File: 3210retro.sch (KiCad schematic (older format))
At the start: 11 parts, among them P101 USB_OTG, P102 NIMH, P103 LIPO, P104 DC, P105 EAR, P106 SPEAKER, P107 HEADPHONE, P108 RUMBLE, X101 ANT_GPS, X102 ANT_GSM

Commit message: Modification for STM32 adaption
For the Hackaday Prize 2017 I decided to switch to STM32 as CPU

*Power system was modified to just contain the charge IC,
*Boost converter for high voltage peripherals
*Buck converter for 3V3 for CPU and switchable NVCC_3V3
   for peripherie

CPU signals are routed and pinmux is done in firmware folder.

SD-Card has 4bit Interface

WiFi module ESP8266 is connected via UART

Wolfson Ausio codec is connected via SAI

Two digital microphones for noise canceling

Rumble Motor driver

LCD is connected via it's own I2C interface
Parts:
- removed P102: NIMH, Pin_Headers:Pin_Header_Straight_2x01, symbol CONN_01X02
- added TP101: TP, NokiaRetroFit:TP, symbol TP
- R101: footprint Resistors_SMD:R_0402 -> Resistors_SMD:R_0402_NoSilk
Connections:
- wire segments 61 -> 85
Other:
- note added: "CPU"
- note added: "Debug UART Output"
- note added: "IMU"
- note added: "Power management and battery charger circuit"
- note added: "SD-Card"
- note removed: "11"
- note removed: "12"
- note removed: "13"
- note removed: "8,9,10,11,12,13"
- note removed: "Battery selection and power domain overview"
- note removed: "CPU mainsheet"
- note removed: "DDR3 RAM"
- note removed: "SD interface / eMMC"
- note removed: "USB / IMU (gyro, accel, comp)"
- note removed: "i.MX7 PMIC"
- note removed: "i.MX7 power"
- moved on the sheet: P103

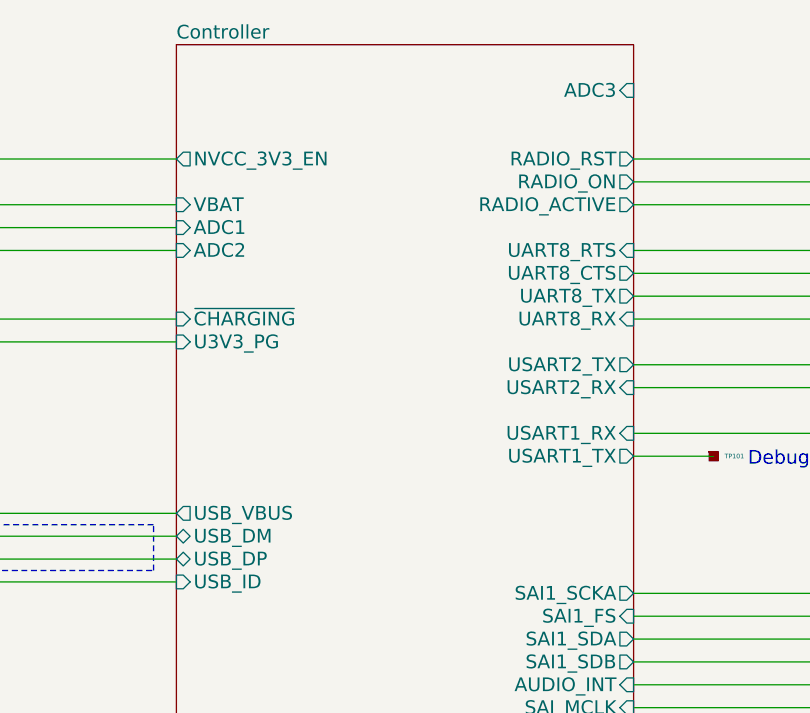
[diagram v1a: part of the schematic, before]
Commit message: Placed a lot of components and routed the audio codec
The BGA of tha audio chipset is to small for regualr technology.
We do not use all of the pins of the chip so we ignore the other
pads and escape throug the balls of the other pad.
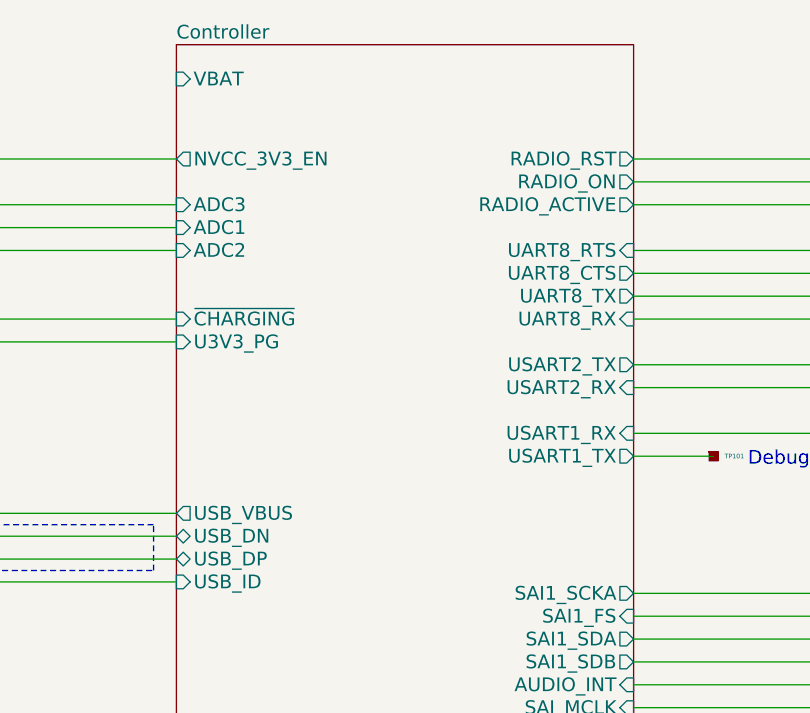
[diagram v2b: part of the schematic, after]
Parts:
- P107: footprint Pin_Headers:Pin_Header_Straight_1x05 -> NokiaRetroFit:PJ_320_D
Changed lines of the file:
@@
 LIBS:contrib
 LIBS:valves
-LIBS:tps62742
-LIBS:WM8994ECS
+LIBS:stm32
 LIBS:3210retro-cache
 EELAYER 26 0
@@
 F14 "ADC1" I L 5650 2350 60
 F15 "ADC2" I L 5650 2450 60
-F16 "ADC3" I R 7650 1750 60
+F16 "ADC3" I L 5650 2250 60
 F17 "I2C3_SCL" O L 5650 7300 60
 F18 "USART1_TX" O R 7650 3350 60
@@
 F27 "USB_ID" I L 5650 3900 60
 F28 "USB_VBUS" O L 5650 3600 60
-F29 "USB_DM" B L 5650 3700 60
-F30 "USB_DP" B L 5650 3800 60
-F31 "RTC_TS" O R 7650 7250 60
-F32 "USART6_TX" O R 7650 9200 60
-F33 "USART6_RX" I R 7650 9300 60
-F34 "SD_D0" B L 5650 6250 60
-F35 "I2C3_SDA" B L 5650 7400 60
-F36 "SD_CK" O L 5650 6050 60
-F37 "ETC_ALARM" O R 7650 7350 60
-F38 "VBAT" I L 5650 2250 60
-F39 "TIM10_PWM" O R 7650 10250 60
-F40 "JTAG_RST" I L 5650 8900 60
-F41 "I2C1_SDA" B L 5650 9950 60
-F42 "LCD_RS" O L 5650 7600 60
-F43 "LCD_RESET" O L 5650 8150 60
-F44 "~CHARGING" I L 5650 2750 60
-F45 "IMU_DRDY_M" I L 5650 9450 60
-F46 "IMU_INT_M" I L 5650 9550 60
-F47 "IMU_INT2" I L 5650 9650 60
-F48 "IMU_INT1" I L 5650 9750 60
-F49 "IMU_EN" O L 5650 9300 60
-F50 "UART8_CTS" O R 7650 2550 60
-F51 "UART8_RTS" I R 7650 2450 60
-F52 "RADIO_ACTIVE" O R 7650 2250 60
-F53 "RADIO_RST" O R 7650 2050 60
-F54 "WIFI_CHPD" O R 7650 8900 60
-F55 "WIFI_RESET" O R 7650 9000 60
-F56 "WIFI_BOOT0" O R 7650 9500 60
-F57 "RADIO_ON" O R 7650 2150 60
-F58 "NVCC_3V3_EN" O L 5650 2050 60
-F59 "U3V3_PG" I L 5650 2850 60
-F60 "SAI1_SCKA" O R 7650 3950 60
-F61 "SAI1_SDA" O R 7650 4150 60
-F62 "SAI1_SDB" O R 7650 4250 60
-F63 "AUDIO_INT" I R 7650 4350 60
-F64 "RUMBLE_EN" O R 7650 6850 60
-F65 "TIM11_RUMBLE_PWM" O R 7650 6950 60
-F66 "SD_D1" B L 5650 6350 60
-F67 "SD_D2" B L 5650 6450 60
-F68 "SD_D3" B L 5650 6550 60
-F69 "PE7" B L 5650 5000 60
-F70 "PE8" B L 5650 5100 60
-F71 "PE9" B L 5650 5200 60
-F72 "PE10" B L 5650 5300 60
+F29 "USB_DP" B L 5650 3800 60
+F30 "RTC_TS" O R 7650 7250 60
+F31 "USART6_TX" O R 7650 9200 60
+F32 "USART6_RX" I R 7650 9300 60
+F33 "SD_D0" B L 5650 6250 60
+F34 "I2C3_SDA" B L 5650 7400 60
+F35 "SD_CK" O L 5650 6050 60
+F36 "ETC_ALARM" O R 7650 7350 60
+F37 "VBAT" I L 5650 1700 60
+F38 "TIM10_PWM" O R 7650 10250 60
+F39 "JTAG_RST" I L 5650 8900 60
+F40 "I2C1_SDA" B L 5650 9950 60
+F41 "LCD_RS" O L 5650 7600 60
+F42 "LCD_RESET" O L 5650 8150 60
+F43 "~CHARGING" I L 5650 2750 60
+F44 "IMU_DRDY_M" I L 5650 9450 60
+F45 "IMU_INT_M" I L 5650 9550 60
+F46 "IMU_INT2" I L 5650 9650 60
+F47 "IMU_INT1" I L 5650 9750 60
+F48 "IMU_EN" O L 5650 9300 60
+F49 "UART8_CTS" O R 7650 2550 60
+F50 "UART8_RTS" I R 7650 2450 60
+F51 "RADIO_ACTIVE" O R 7650 2250 60
+F52 "RADIO_RST" O R 7650 2050 60
+F53 "WIFI_CHPD" O R 7650 8900 60
+F54 "WIFI_RESET" O R 7650 9000 60
+F55 "WIFI_BOOT0" O R 7650 9500 60
+F56 "RADIO_ON" O R 7650 2150 60
+F57 "NVCC_3V3_EN" O L 5650 2050 60
+F58 "U3V3_PG" I L 5650 2850 60
+F59 "SAI1_SCKA" O R 7650 3950 60
+F60 "SAI1_SDA" O R 7650 4150 60
+F61 "SAI1_SDB" O R 7650 4250 60
+F62 "AUDIO_INT" I R 7650 4350 60
+F63 "RUMBLE_EN" O R 7650 6850 60
+F64 "TIM11_RUMBLE_PWM" O R 7650 6950 60
+F65 "SD_D1" B L 5650 6350 60
+F66 "SD_D2" B L 5650 6450 60
+F67 "SD_D3" B L 5650 6550 60
+F68 "PE7" B L 5650 5000 60
+F69 "PE8" B L 5650 5100 60
+F70 "PE9" B L 5650 5200 60
+F71 "PE10" B L 5650 5300 60
+F72 "USB_DN" B L 5650 3700 60
 $EndSheet
 $Comp
@@
 F 0 "P107" H 15000 4000 50  0000 C CNN
 F 1 "HEADPHONE" H 15100 3700 59  0000 L CNB
-F 2 "Pin_Headers:Pin_Header_Straight_1x05" H 15000 3700 50  0001 C CNN
+F 2 "NokiaRetroFit:PJ_320_D" H 15000 3700 50  0001 C CNN
 F 3 "" H 15000 3700 50  0000 C CNN
 	1    15000 3700

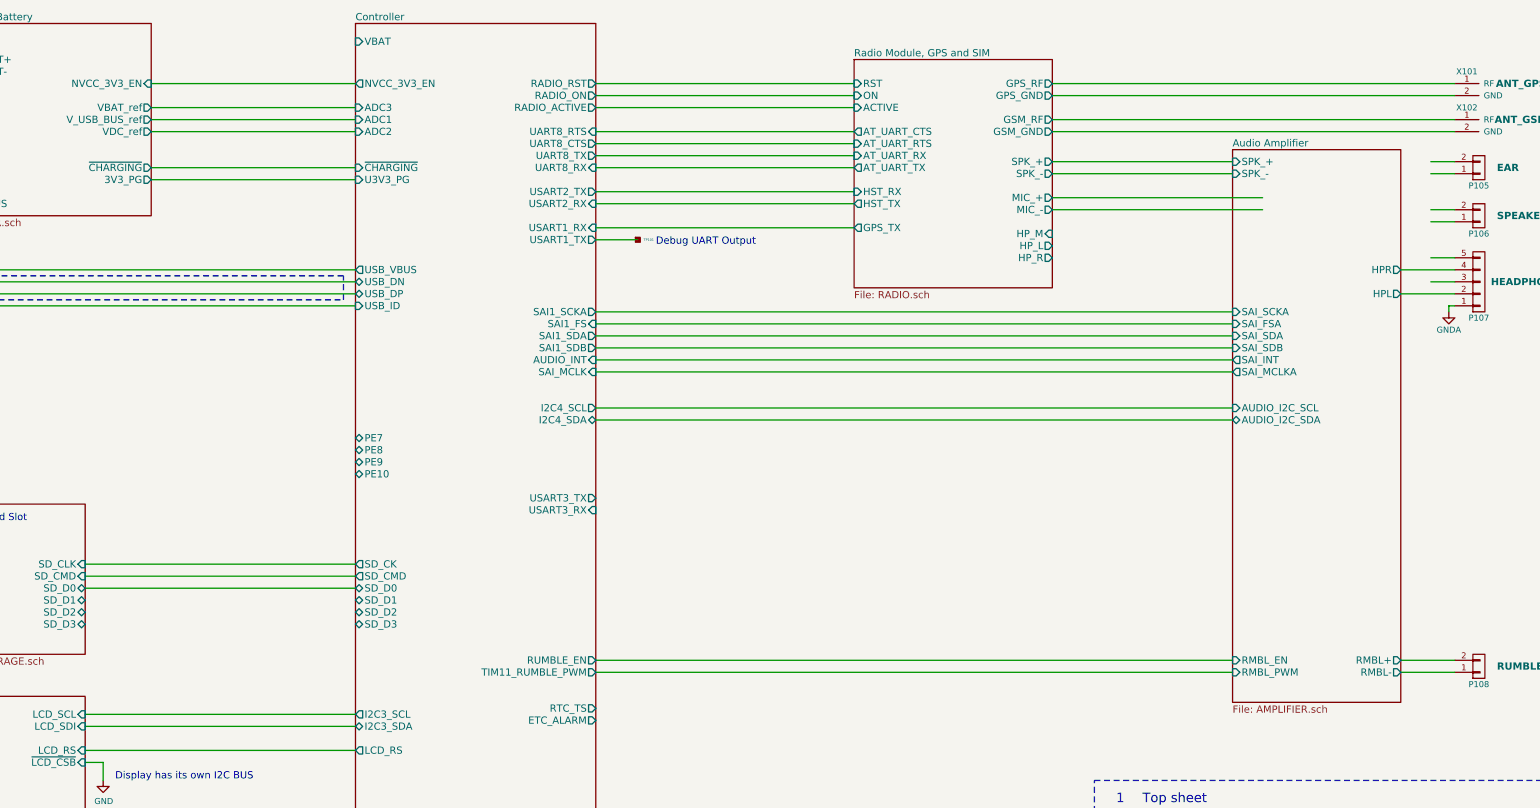
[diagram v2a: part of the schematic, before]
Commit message: Revision 1 of Layout
6layer board
through-hole via only (0.5/0.3mm drill)
0.2mm track width

https://hackaday.io/project/21263-nokia-3210-retro-fit-board/log/66914-prototype-pcb-done-there-comes-the-review
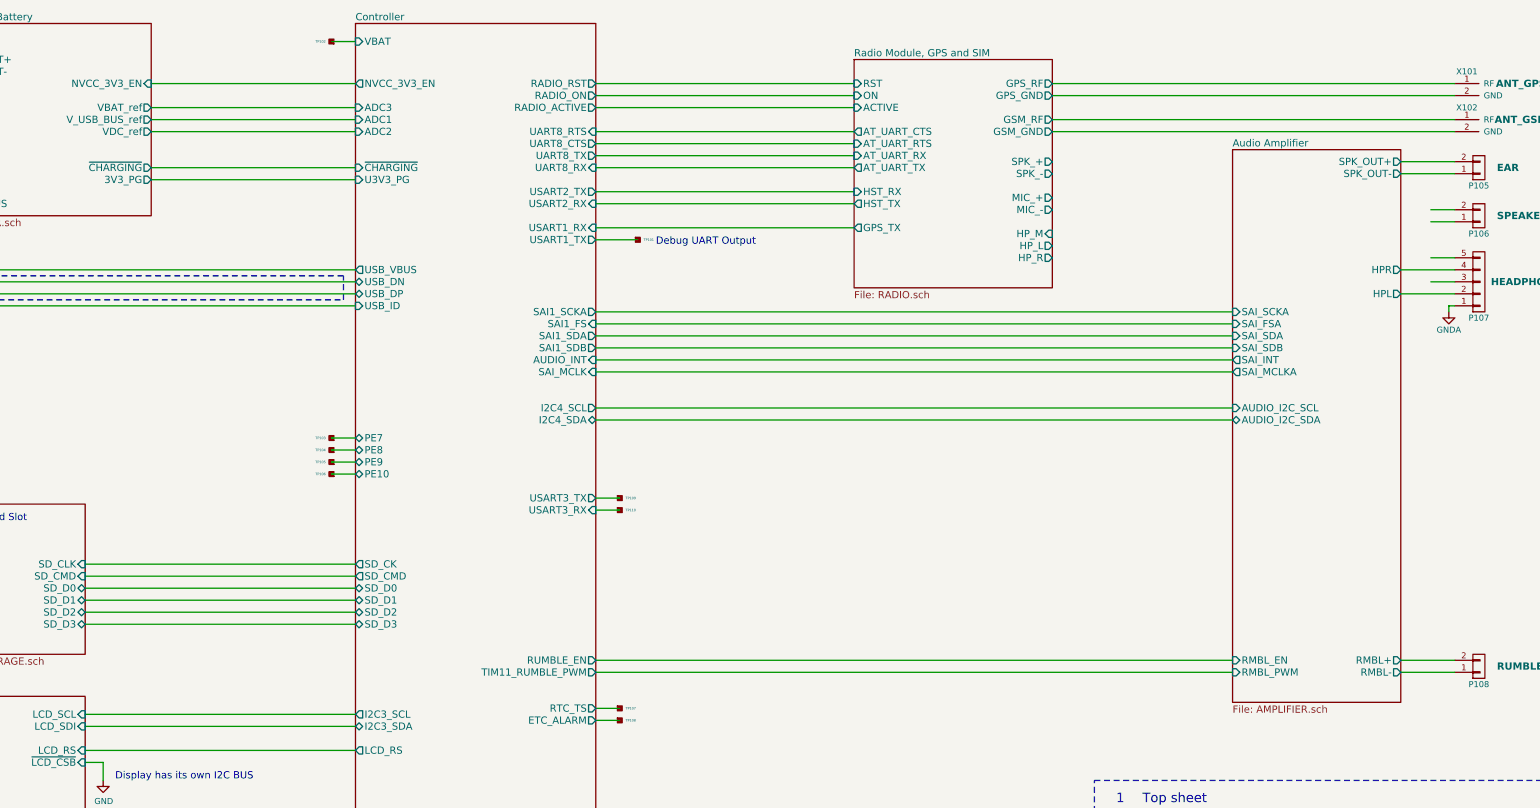
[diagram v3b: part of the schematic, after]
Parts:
- added TP102, TP103, TP104, TP105, TP106, TP107, TP108, TP109, TP110: TP, NokiaRetroFit:TP, symbol TP
- P103, P104, P105, P106: footprint Pin_Headers:Pin_Header_Straight_2x01 -> NokiaRetroFit:SolderWirePad_2x_0,8
- P108: footprint Pin_Headers:Pin_Header_Straight_1x02 -> buttons:Rumble_Pads
- X101, X102: footprint SMD_Packages:1Pin -> NokiaRetroFit:SolderWirePad_2x_0,8
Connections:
- wire segments 85 -> 93
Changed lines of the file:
@@
 F 0 "P103" H 1700 2050 50  0000 C CNN
 F 1 "LIPO" V 1800 1900 50  0000 C CNN
-F 2 "Pin_Headers:Pin_Header_Straight_2x01" H 1700 1900 50  0001 C CNN
+F 2 "NokiaRetroFit:SolderWirePad_2x_0,8" H 1700 1900 50  0001 C CNN
 F 3 "" H 1700 1900 50  0000 C CNN
 	1    1700 1900
@@
 F8 "AUDIO_I2C_SCL" I L 12950 4750 60
 F9 "AUDIO_I2C_SDA" B L 12950 4850 60
-F10 "SPK_+" I L 12950 2700 60
-F11 "SPK_-" I L 12950 2800 60
-F12 "SAI_SCKA" I L 12950 3950 60
-F13 "SAI_FSA" I L 12950 4050 60
-F14 "SAI_SDA" I L 12950 4150 60
-F15 "SAI_SDB" I L 12950 4250 60
-F16 "SAI_INT" O L 12950 4350 60
-F17 "SAI_MCLKA" O L 12950 4450 60
+F10 "SAI_SCKA" I L 12950 3950 60
+F11 "SAI_FSA" I L 12950 4050 60
+F12 "SAI_SDA" I L 12950 4150 60
+F13 "SAI_SDB" I L 12950 4250 60
+F14 "SAI_INT" O L 12950 4350 60
+F15 "SAI_MCLKA" O L 12950 4450 60
+F16 "SPK_OUT+" O R 14350 2700 60
+F17 "SPK_OUT-" O R 14350 2800 60
 $EndSheet
 $Comp
@@
 F 0 "P105" H 15000 2900 50  0000 C CNN
 F 1 "EAR" H 15150 2750 60  0000 L CNB
-F 2 "Pin_Headers:Pin_Header_Straight_2x01" H 15000 2750 50  0001 C CNN
+F 2 "NokiaRetroFit:SolderWirePad_2x_0,8" H 15000 2750 50  0001 C CNN
 F 3 "" H 15000 2750 50  0000 C CNN
 	1    15000 2750
@@
 $EndComp
 Wire Wire Line
-	14600 2700 14800 2700
-Wire Wire Line
-	14600 2800 14800 2800
-$Comp
-L GNDA #PWR01
-U 1 1 58075318
-P 14750 3950
-F 0 "#PWR01" H 14750 3700 50  0001 C CNN
-F 1 "GNDA" H 14750 3800 50  0000 C CNN
-F 2 "" H 14750 3950 50  0000 C CNN
-F 3 "" H 14750 3950 50  0000 C CNN
-	1    14750 3950
-	1    0    0    -1
-$EndComp
+	14350 2700 14800 2700
+Wire Wire Line
+	14350 2800 14800 2800
 Wire Wire Line
 	14750 3900 14800 3900
@@
 F 0 "X102" H 14900 2450 50  0000 C CNN
 F 1 "ANT_GSM" H 15350 2350 60  0000 C CNB
-F 2 "SMD_Packages:1Pin" H 14800 2350 60  0001 C CNN
+F 2 "NokiaRetroFit:SolderWirePad_2x_0,8" H 14800 2350 60  0001 C CNN
 F 3 "" H 14800 2350 60  0000 C CNN
 	1    14800 2350
@@
 F 0 "X101" H 14900 2150 50  0000 C CNN
 F 1 "ANT_GPS" H 15350 2050 60  0000 C CNB
-F 2 "SMD_Packages:1Pin" H 14800 2050 60  0001 C CNN
+F 2 "NokiaRetroFit:SolderWirePad_2x_0,8" H 14800 2050 60  0001 C CNN
 F 3 "" H 14800 2050 60  0000 C CNN
 	1    14800 2050
@@
 F 0 "P104" H 1700 2850 50  0000 C CNN
 F 1 "DC" V 1800 2700 50  0000 C CNN
-F 2 "Pin_Headers:Pin_Header_Straight_2x01" H 1700 2700 50  0001 C CNN
+F 2 "NokiaRetroFit:SolderWirePad_2x_0,8" H 1700 2700 50  0001 C CNN
 F 3 "" H 1700 2700 50  0000 C CNN
 	1    1700 2700
@@
 F 0 "P108" H 15000 7050 50  0000 C CNN
 F 1 "RUMBLE" H 15150 6900 60  0000 L CNB
-F 2 "Pin_Headers:Pin_Header_Straight_1x02" H 15000 6900 50  0001 C CNN
+F 2 "buttons:Rumble_Pads" H 15000 6900 50  0001 C CNN
 F 3 "" H 15000 6900 50  0000 C CNN
 	1    15000 6900
@@
 Text Notes 2250 3800 0    59   ~ 0
 50 Ohm
-Wire Wire Line
-	12950 2700 11450 2700
-Wire Wire Line
-	11450 2800 12950 2800
-Wire Wire Line
-	13200 3000 11450 3000
-Wire Wire Line
-	11450 3100 13200 3100
 Wire Bus Line
 	7650 10550 9000 10550
@@
 F 0 "P106" H 15000 3300 50  0000 C CNN
 F 1 "SPEAKER" H 15150 3150 60  0000 L CNB
-F 2 "Pin_Headers:Pin_Header_Straight_2x01" H 15000 3150 50  0001 C CNN
+F 2 "NokiaRetroFit:SolderWirePad_2x_0,8" H 15000 3150 50  0001 C CNN
 F 3 "" H 15000 3150 50  0000 C CNN
 	1    15000 3150
@@
 Wire Notes Line
 	11800 7850 16050 7850
+$Comp
+L TP TP102
+U 1 1 59B5703E
+P 5450 1700
+F 0 "TP102" H 5498 1700 20  0000 L CNN
+F 1 "TP" H 5450 1650 60  0001 C CNN
+F 2 "NokiaRetroFit:TP" H 5450 1700 60  0001 C CNN
+F 3 "" H 5450 1700 60  0000 C CNN
+	1    5450 1700
+	-1   0    0    1
+$EndComp
+Wire Wire Line
+	5450 1700 5650 1700
+$Comp
+L TP TP108
+U 1 1 59B58A3B
+P 7850 7350
+F 0 "TP108" H 7898 7350 20  0000 L CNN
+F 1 "TP" H 7850 7300 60  0001 C CNN
+F 2 "NokiaRetroFit:TP" H 7850 7350 60  0001 C CNN
+F 3 "" H 7850 7350 60  0000 C CNN
+	1    7850 7350
+	1    0    0    -1
+$EndComp
+$Comp
+L TP TP107
+U 1 1 59B59F7A
+P 7850 7250
+F 0 "TP107" H 7898 7250 20  0000 L CNN
+F 1 "TP" H 7850 7200 60  0001 C CNN
+F 2 "NokiaRetroFit:TP" H 7850 7250 60  0001 C CNN
+F 3 "" H 7850 7250 60  0000 C CNN
+	1    7850 7250
+	1    0    0    -1
+$EndComp
+$Comp
+L TP TP106
+U 1 1 59B5A312
+P 5450 5300
+F 0 "TP106" H 5498 5300 20  0000 L CNN
+F 1 "TP" H 5450 5250 60  0001 C CNN
+F 2 "NokiaRetroFit:TP" H 5450 5300 60  0001 C CNN
+F 3 "" H 5450 5300 60  0000 C CNN
+	1    5450 5300
+	-1   0    0    1
+$EndComp
+$Comp
+L TP TP105
+U 1 1 59B5B3A3
+P 5450 5200
+F 0 "TP105" H 5498 5200 20  0000 L CNN
+F 1 "TP" H 5450 5150 60  0001 C CNN
+F 2 "NokiaRetroFit:TP" H 5450 5200 60  0001 C CNN
+F 3 "" H 5450 5200 60  0000 C CNN
+	1    5450 5200
+	-1   0    0    1
+$EndComp
+$Comp
+L TP TP104
+U 1 1 59B5B73F
+P 5450 5100
+F 0 "TP104" H 5498 5100 20  0000 L CNN
+F 1 "TP" H 5450 5050 60  0001 C CNN
+F 2 "NokiaRetroFit:TP" H 5450 5100 60  0001 C CNN
+F 3 "" H 5450 5100 60  0000 C CNN
+	1    5450 5100
+	-1   0    0    1
+$EndComp
+$Comp
+L TP TP103
+U 1 1 59B5BADD
+P 5450 5000
+F 0 "TP103" H 5498 5000 20  0000 L CNN
+F 1 "TP" H 5450 4950 60  0001 C CNN
+F 2 "NokiaRetroFit:TP" H 5450 5000 60  0001 C CNN
+F 3 "" H 5450 5000 60  0000 C CNN
+	1    5450 5000
+	-1   0    0    1
+$EndComp
+Wire Wire Line
+	5650 5000 5450 5000
+Wire Wire Line
+	5450 5100 5650 5100
+Wire Wire Line
+	5650 5200 5450 5200
+Wire Wire Line
+	5450 5300 5650 5300
+Wire Wire Line
+	7850 7250 7650 7250
+Wire Wire Line
+	7650 7350 7850 7350
+$Comp
+L TP TP110
+U 1 1 59B5F8E6
+P 7850 5600
+F 0 "TP110" H 7898 5600 20  0000 L CNN
+F 1 "TP" H 7850 5550 60  0001 C CNN
+F 2 "NokiaRetroFit:TP" H 7850 5600 60  0001 C CNN
+F 3 "" H 7850 5600 60  0000 C CNN
+	1    7850 5600
+	1    0    0    -1
+$EndComp
+$Comp
+L TP TP109
+U 1 1 59B5F8EC
+P 7850 5500
+F 0 "TP109" H 7898 5500 20  0000 L CNN
+F 1 "TP" H 7850 5450 60  0001 C CNN
+F 2 "NokiaRetroFit:TP" H 7850 5500 60  0001 C CNN
+F 3 "" H 7850 5500 60  0000 C CNN
+	1    7850 5500
+	1    0    0    -1
+$EndComp
+Wire Wire Line
+	7850 5500 7650 5500
+Wire Wire Line
+	7650 5600 7850 5600
+$Comp
+L GNDA #PWR01
+U 1 1 58075318
+P 14750 3950
+F 0 "#PWR01" H 14750 3700 50  0001 C CNN
+F 1 "GNDA" H 14750 3800 50  0000 C CNN
+F 2 "" H 14750 3950 50  0000 C CNN
+F 3 "" H 14750 3950 50  0000 C CNN
+	1    14750 3950
+	1    0    0    -1
+$EndComp
+Wire Wire Line
+	3400 6350 5650 6350
+Wire Wire Line
+	3400 6450 5650 6450
+Wire Wire Line
+	3400 6550 5650 6550
 $EndSCHEMATC
